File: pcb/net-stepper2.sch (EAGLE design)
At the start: 38 parts, among them J1 MICRO-USB, J2 POWER_JACKPTH_LOCK, J3 ENCODER, J4 ENDSTOP2, J5 ENDSTOP1, J6 STEPER, Q1 600mA/40V, Q2 600mA/40V, U1 L6470, U2 CP2104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

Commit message: remapped pins
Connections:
- net ADC renamed SC_ADC
- net CSN renamed SC_CSN
- net DTR renamed ESP_DTR
- net OUT1A renamed SC_OUT1A
- net OUT1B renamed SC_OUT1B
- net OUT2A renamed SC_OUT2A
- net OUT2B renamed SC_OUT2B
- net PGRM renamed ESP_PGRM
- net RESET renamed ESP_RESET
- net RESETN renamed SC_RESETN
- net RTS renamed ESP_RTS
- net RX renamed ESP_RX
- net SCK renamed SC_SCK
- net SDI renamed SC_SDI
- net SDO renamed SC_SDO
- net TX renamed ESP_TX
- removed net BLUE: R12.2, U2G$1.GPIO1/RXLED, U5.35-IA
- removed net DOWN: S1.P$1, U5.26-IOD
- removed net END_STOP_1: J5.2, U5.15
- removed net END_STOP_2: J4.2, U5.17-IO
- removed net GREEN: R11.2, U2G$1.GPIO0/TXLED, U5.34-IA
- removed net HOME: S4.P$1, U5.27-IO
- removed net RED: R6.2, U5.32-IOA
- removed net STOP: S3.P$1, U5.12
- removed net UP: S2.P$1, U5.33-IOA
- new net BTN_DOWN: S1.P$1, U5.4-IO
- new net BTN_HOME: S4.P$1, U5.13-IO
- new net BTN_STOP: S3.P$1, U5.15
- new net BTN_UP: S2.P$1, U5.17-IO, U5.25-IOD
- new net ENDS_1: J5.2, U5.32-IOA
- new net ENDS_2: J4.2, U5.33-IOA
- new net LED_BLUE: R12.2, U2G$1.GPIO1/RXLED, U5.14-IO
- new net LED_GREEN: R11.2, U2G$1.GPIO0/TXLED, U5.27-IO
- new net LED_RED: R6.2, U5.26-IOD
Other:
- moved on the sheet: U2G$2

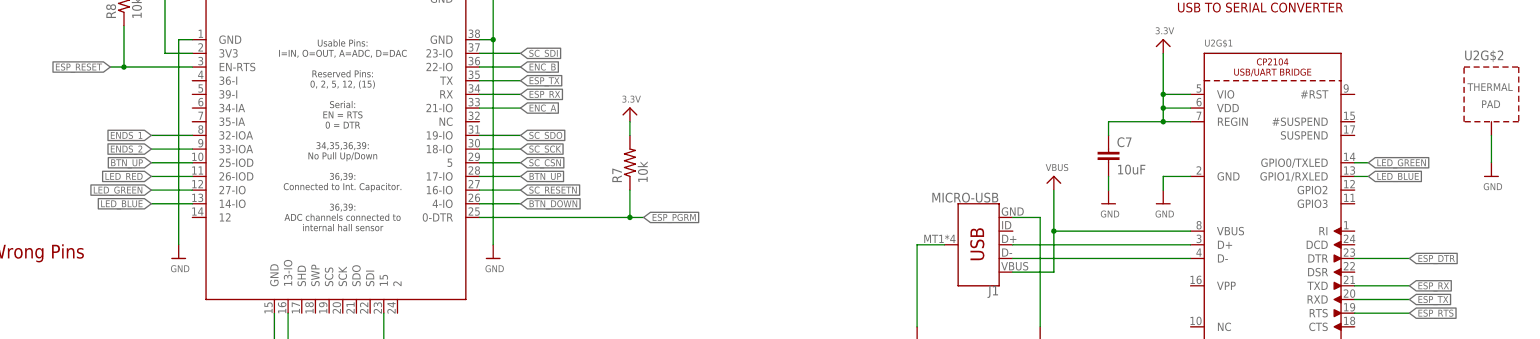
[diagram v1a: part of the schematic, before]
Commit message: prepared new routing
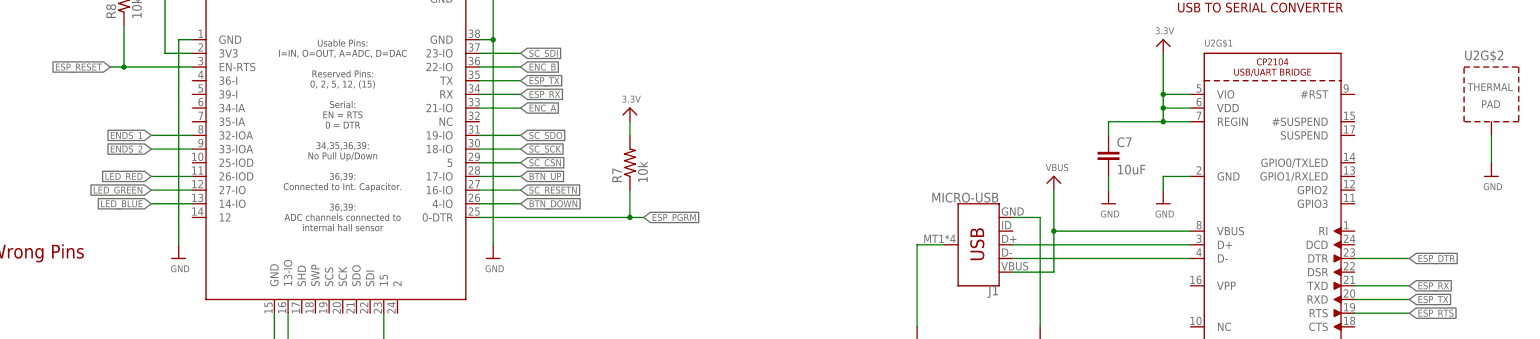
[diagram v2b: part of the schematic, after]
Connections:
- net BTN_UP: no longer U5.25-IOD
- net LED_BLUE: no longer U2G$1.GPIO1/RXLED
- net LED_GREEN: no longer U2G$1.GPIO0/TXLED
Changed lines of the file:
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@@
-</segment>
-<segment>
-<pinref part="U5" gate="G$1" pin="25-IOD"/>
-<wire x1="292.1" y1="129.54" x2="284.48" y2="129.54" width="0.1524" layer="91"/>
-<label x="284.48" y="129.54" size="1.27" layer="95" rot="R180" xref="yes"/>
 </segment>
 <segment>
@@
 </segment>
 <segment>
-<label x="510.54" y="129.54" size="1.27" layer="95" xref="yes"/>
-<pinref part="U2" gate="G$1" pin="GPIO0/TXLED"/>
-<wire x1="508" y1="129.54" x2="510.54" y2="129.54" width="0.1524" layer="91"/>
-</segment>
-<segment>
 <pinref part="U5" gate="G$1" pin="27-IO"/>
 <wire x1="292.1" y1="124.46" x2="284.48" y2="124.46" width="0.1524" layer="91"/>
@@
 </segment>
 <segment>
-<label x="510.54" y="127" size="1.27" layer="95" xref="yes"/>
-<pinref part="U2" gate="G$1" pin="GPIO1/RXLED"/>
-<wire x1="508" y1="127" x2="510.54" y2="127" width="0.1524" layer="91"/>
-</segment>
-<segment>

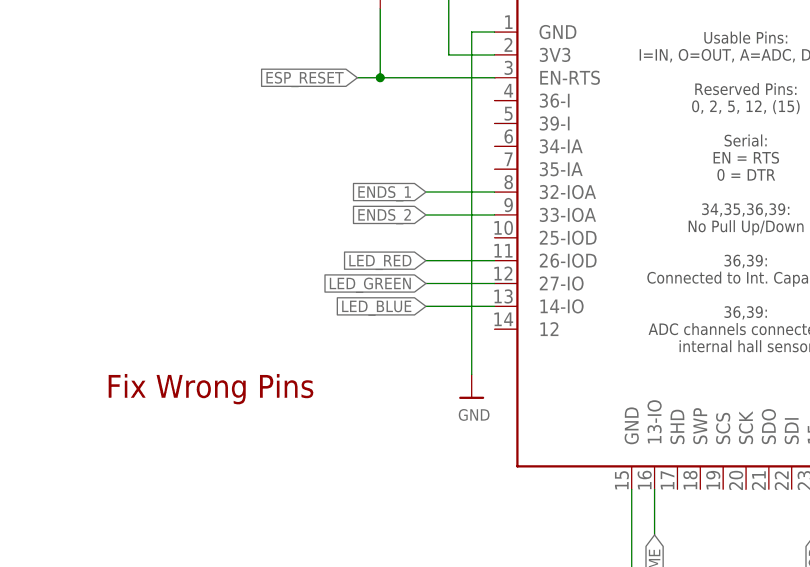
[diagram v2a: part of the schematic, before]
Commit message: Missing routing fixed
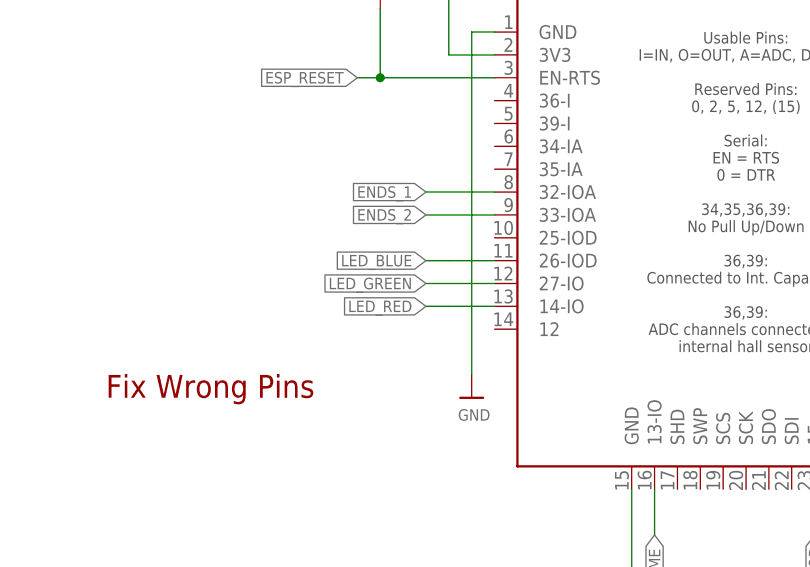
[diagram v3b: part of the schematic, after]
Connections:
- net LED_BLUE: now also U5.26-IOD; no longer U5.14-IO
- net LED_RED: now also U5.14-IO; no longer U5.26-IOD
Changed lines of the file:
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@@
 </segment>
 <segment>
-<pinref part="U5" gate="G$1" pin="26-IOD"/>
-<wire x1="292.1" y1="127" x2="284.48" y2="127" width="0.1524" layer="91"/>
-<label x="284.48" y="127" size="1.27" layer="95" rot="R180" xref="yes"/>
+<label x="284.48" y="121.92" size="1.27" layer="95" rot="R180" xref="yes"/>
+<wire x1="287.02" y1="121.92" x2="284.48" y2="121.92" width="0.1524" layer="91"/>
+<wire x1="287.02" y1="121.92" x2="292.1" y2="121.92" width="0.1524" layer="91"/>
+<pinref part="U5" gate="G$1" pin="14-IO"/>
 </segment>
 </net>
@@
 </segment>
 <segment>
-<pinref part="U5" gate="G$1" pin="14-IO"/>
-<wire x1="292.1" y1="121.92" x2="284.48" y2="121.92" width="0.1524" layer="91"/>
-<label x="284.48" y="121.92" size="1.27" layer="95" rot="R180" xref="yes"/>
+<label x="284.48" y="127" size="1.27" layer="95" rot="R180" xref="yes"/>
+<wire x1="287.02" y1="127" x2="284.48" y2="127" width="0.1524" layer="91"/>
+<wire x1="287.02" y1="127" x2="292.1" y2="127" width="0.1524" layer="91"/>
+<pinref part="U5" gate="G$1" pin="26-IOD"/>
 </segment>
 </net>

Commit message: removed todo
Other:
- note removed: "Fix Wrong Pins"
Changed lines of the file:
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@@
 <text x="474.98" y="157.48" size="1.778" layer="94">USB TO SERIAL CONVERTER</text>
 <text x="205.74" y="25.4" size="1.778" layer="94">RGB LED</text>
-<text x="248.92" y="111.76" size="2.54" layer="94" font="vector" ratio="20">Fix Wrong Pins</text>
 </plain>
 <instances>
